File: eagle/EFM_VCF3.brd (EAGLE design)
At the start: 102.2 x 80.9 mm, 44 parts, among them IC1 LM13700N, IC2 TL084P, Q3 2N3906, Q4 2N3906, U1 POWER

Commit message: tweaks and one less jump
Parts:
- moved C2 8.89 mm to (20.3, 47.0)
- moved U1 8.89 mm to (11.4, 41.9)
- moved C1 7.62 mm to (20.3, 40.6)
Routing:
- net +12V: track 248.0 -> 233.0 mm
- net GND: track 474.7 -> 463.7 mm
- net -12V: track 160.4 -> 151.8 mm
- net N$55: track 46.7 -> 39.4 mm
- net N$24: track 126.9 -> 123.2 mm
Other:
- outline, holes or cut-outs redrawn

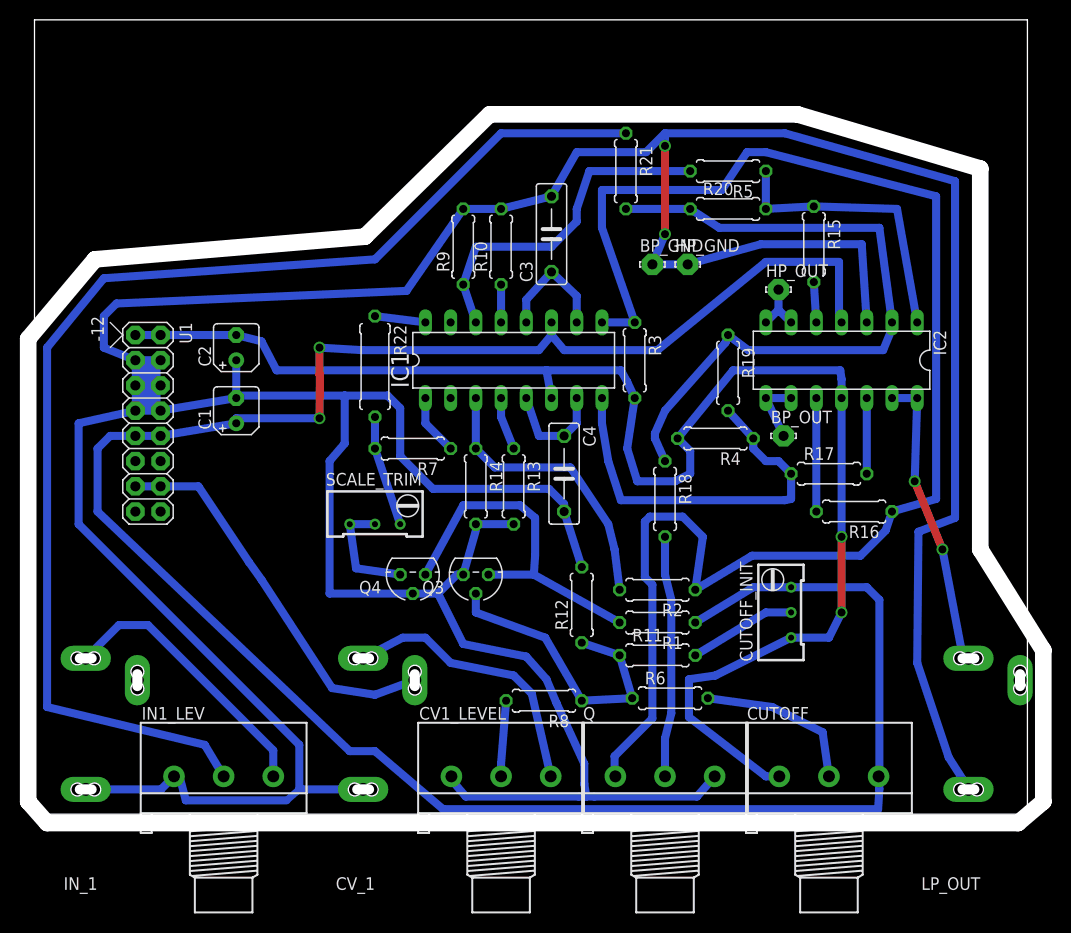
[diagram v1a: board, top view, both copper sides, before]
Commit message: gcode for rectangular cut
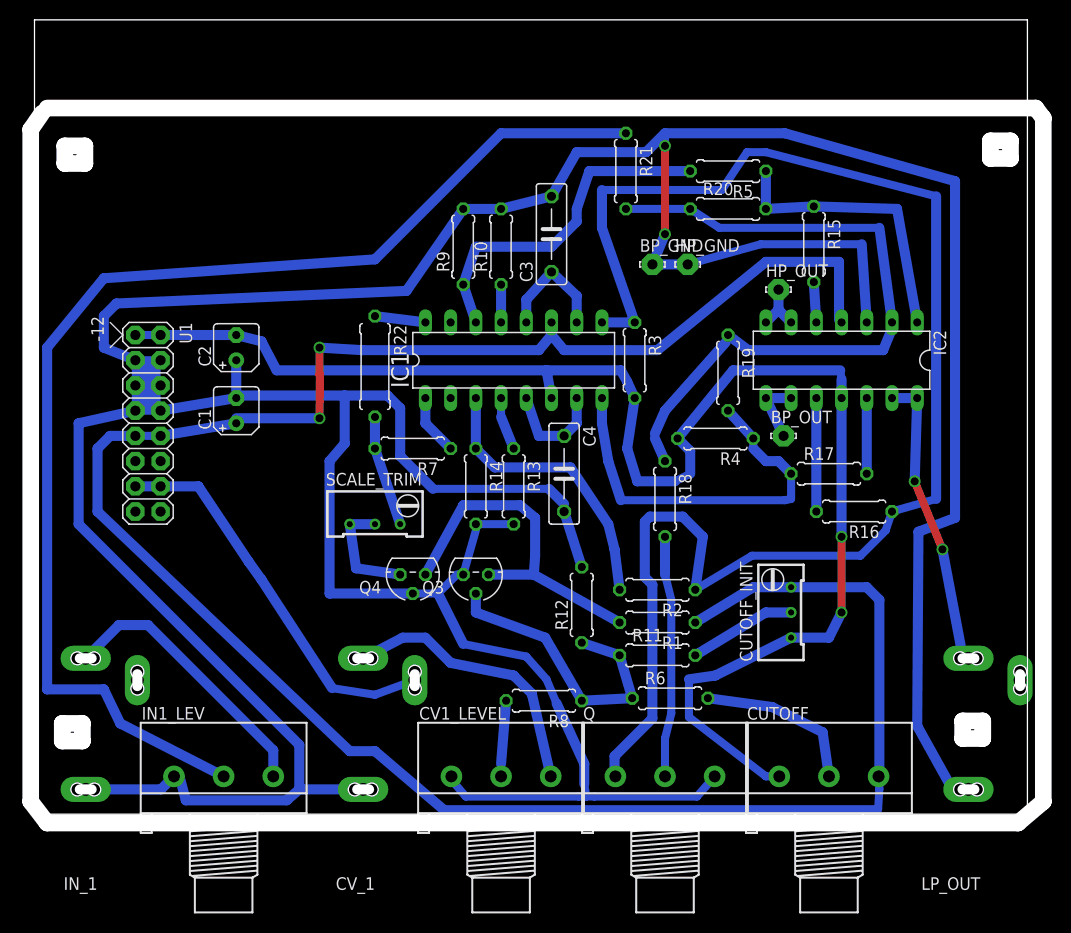
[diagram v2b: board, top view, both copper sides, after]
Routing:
- net GND: track 463.7 -> 465.0 mm
- net N$24: track 123.2 -> 122.6 mm
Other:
- board size 102.2 x 80.9 mm -> 102 x 80.9 mm
